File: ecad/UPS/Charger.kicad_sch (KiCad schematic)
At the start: 73 parts, among them J1 Barrel_Jack, J2 Conn_01x02_Socket, Q1 CSD18540Q5B, Q2 Q_PMOS_DGS, Q4 Q_PMOS_DGS, Q5 CSD18540Q5B, Q6 CSD18540Q5B, Q7 CSD18540Q5B, U1 BQ25730RSNR

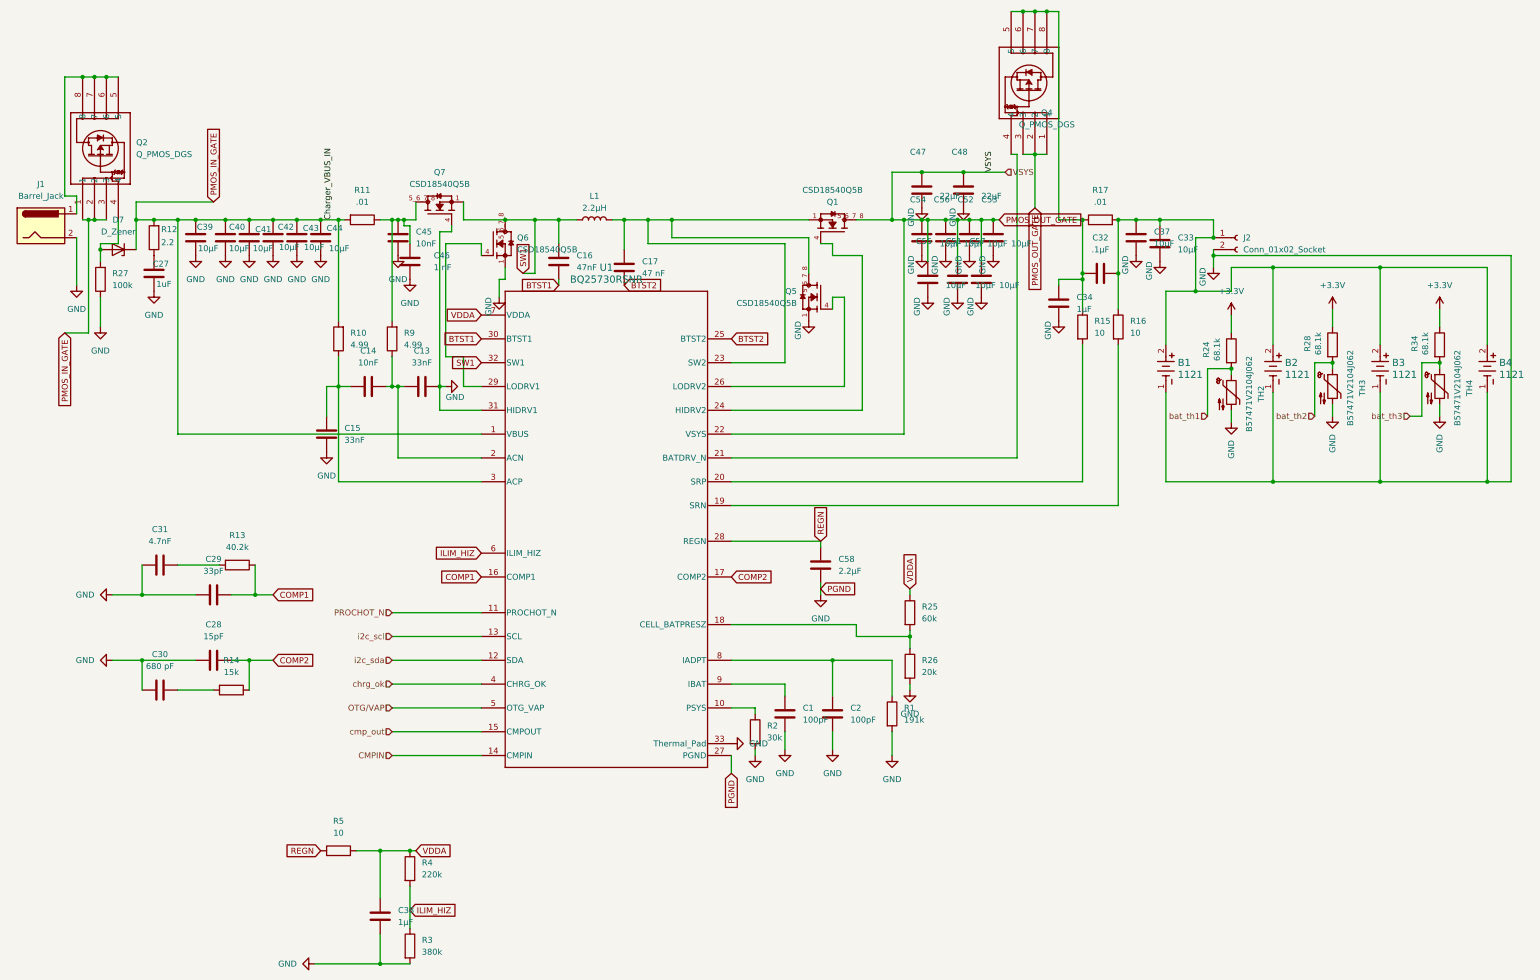
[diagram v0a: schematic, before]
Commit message: Did some routing, need to figure out how to route to BQ while appeasing DRC
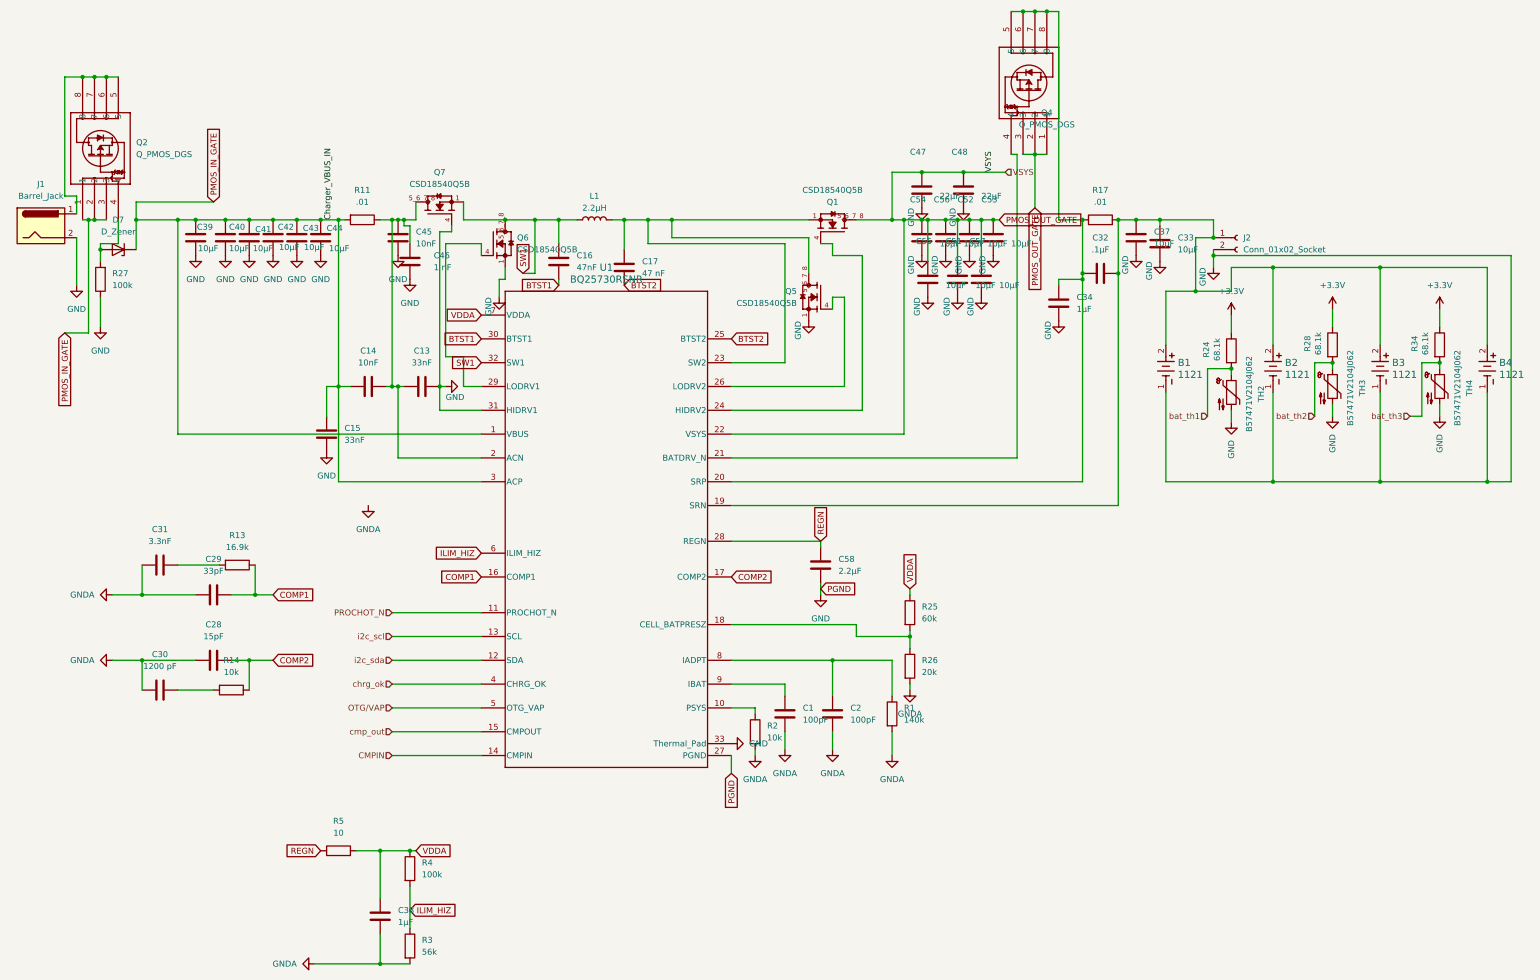
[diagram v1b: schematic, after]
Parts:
- removed C27: 1uF, Capacitor_SMD:C_0603_1608Metric, symbol Device:C
- removed R10, R9: 4.99, Resistor_SMD:R_0805_2012Metric, symbol Device:R
- removed R12: 2.2, Resistor_SMD:R_0805_2012Metric, symbol Device:R
- removed R15, R16: 10, Resistor_SMD:R_0805_2012Metric, symbol Device:R
- C30: value 680 pF -> 1200 pF
- C31: value 4.7nF -> 3.3nF
- Q4: footprint UPS:FDS6681Z_OSI-M -> UPS:FDS6681Z_OSI
- R1: value 191k -> 140k
- R13: value 40.2k -> 16.9k
- R14: value 15k -> 10k
- R2: value 30k -> 10k
- R3: value 380k -> 56k
- R4: value 220k -> 100k
- U1: footprint UPS:RSN0032B-IPC_A -> UPS:RSN0032B-IPC_C
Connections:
- net GND: no longer C1.2, C2.2, C28.1, C29.1, C30.1, C31.1, C38.2, R1.2, R2.2, R26.2, R3.2
- net PMOS_IN_GATE: now also C14.1, C15.2, U1.3 (ACP)
- net at B1.2, B2.2, B3.2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: now also U1.19 (SRN)
- net at C13.1, C14.2, U1.2 (ACN): now also C45.1, C46.1, Q7.5_6_7_8, R11.1
- net at C32.2, C34.1, Q4.5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: now also U1.20 (SRP)
- new net GNDA: C1.2, C2.2, C28.1, C29.1, C30.1, C31.1, C38.2, R1.2, R2.2, R26.2, R3.2

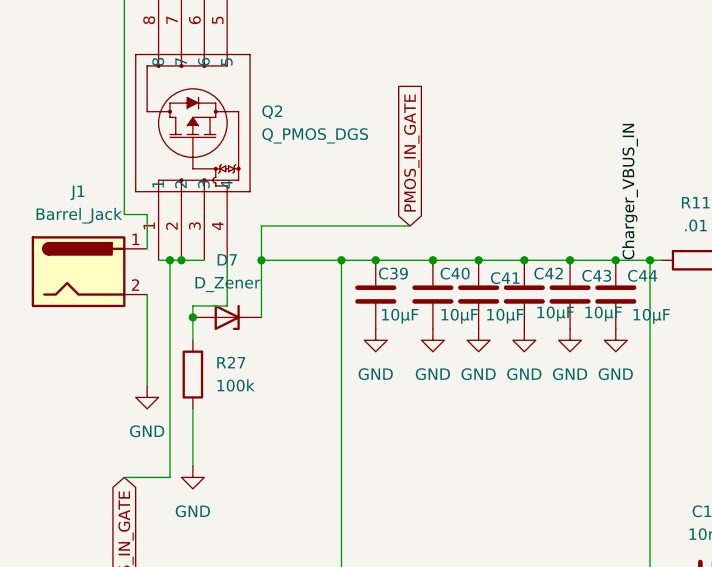
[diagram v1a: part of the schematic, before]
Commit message: Introduce fuses and a bit more routing
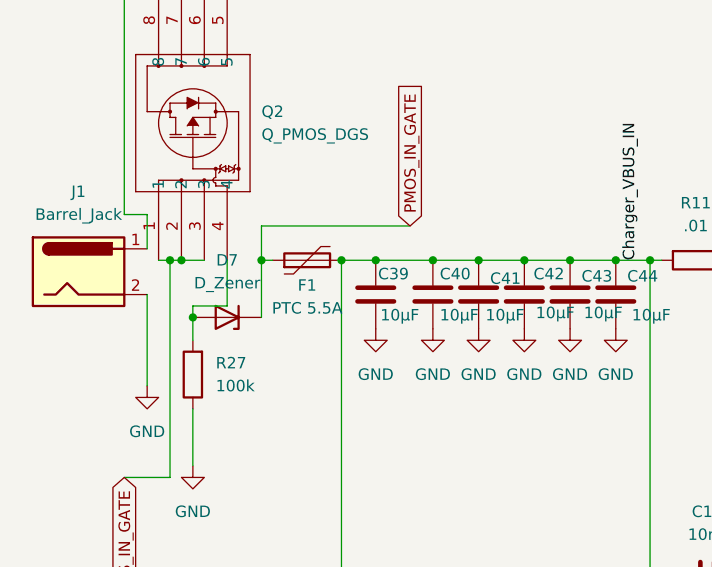
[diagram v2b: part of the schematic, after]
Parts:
- added F1: PTC 5.5A, Fuse:Fuse_1210_3225Metric_Pad1.42x2.65mm_HandSolder, symbol Device:Polyfuse
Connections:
- net PMOS_IN_GATE: now also F1.1; no longer C14.1, C15.2, C39.1, C40.1, C41.1, C42.1, C43.1, C44.1, R11.2, U1.1 (VBUS), U1.3 (ACP)
- new net Charger_VBUS_IN: C14.1, C15.2, C39.1, C40.1, C41.1, C42.1, C43.1, C44.1, F1.2, R11.2, U1.1 (VBUS), U1.3 (ACP)
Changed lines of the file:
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@@
 	)
 	(junction
+		(at 111.76 83.82)
+		(diameter 0)
+		(color 0 0 0 0)
+	)
+	(junction
 		(at 276.86 172.72)
 		(diameter 0)
@@
 	)
 	(junction
+		(at 120.65 83.82)
+		(diameter 0)
+		(color 0 0 0 0)
+	)
+	(junction
 		(at 303.53 69.85)
 		(diameter 0)
@@
 	)
 	(junction
-		(at 111.76 83.82)
-		(diameter 0)
-		(color 0 0 0 0)
-	)
-	(junction
 		(at 341.63 87.63)
 		(diameter 0)
@@
 	)
 	(junction
-		(at 120.65 83.82)
-		(diameter 0)
-		(color 0 0 0 0)
-	)
-	(junction
 		(at 377.19 93.98)
 		(diameter 0)
@@
 	(wire
 		(pts
-			(xy 111.76 83.82) (xy 120.65 83.82)
-		)
-		(stroke
-			(width 0)
-			(type default)
-		)
-	)
-	(wire
-		(pts
 			(xy 345.44 124.46) (xy 345.44 127)
 		)
@@
 	(wire
 		(pts
-			(xy 111.76 90.17) (xy 111.76 83.82)
-		)
-		(stroke
-			(width 0)
-			(type default)
-		)
-	)
-	(wire
-		(pts
 			(xy 177.8 88.9) (xy 185.42 88.9)
 		)
@@
 	(wire
 		(pts
+			(xy 111.76 83.82) (xy 113.03 83.82)
+		)
+		(stroke
+			(width 0)
+			(type default)
+		)
+	)
+	(wire
+		(pts
 			(xy 345.44 93.98) (xy 345.44 99.06)
 		)
@@
 	(wire
 		(pts
+			(xy 111.76 83.82) (xy 111.76 90.17)
+		)
+		(stroke
+			(width 0)
+			(type default)
+		)
+	)
+	(wire
+		(pts
 			(xy 167.64 119.38) (xy 168.91 119.38)
 		)
@@
 					(unit 1)
 				)
+			)
+		)
+	)
+	(symbol
+		(lib_id "Device:Polyfuse")
+		(at 116.84 83.82 90)
+		(unit 1)
+		(exclude_from_sim no)
+		(in_bom yes)
+		(on_board yes)
+		(dnp no)
+		(property "Reference" "F1"
+			(at 116.84 86.614 90)
+			(effects
+				(font
+					(size 1.27 1.27)
+				)
+			)
+		)
+		(property "Value" "PTC 5.5A"
+			(at 116.84 89.154 90)
+			(effects
+				(font
+					(size 1.27 1.27)
+				)
+			)
+		)
+		(property "Footprint" "Fuse:Fuse_1210_3225Metric_Pad1.42x2.65mm_HandSolder"
+			(at 121.92 82.55 0)
+			(effects
+				(font
+					(size 1.27 1.27)
+				)
+				(justify left)
+				(hide yes)
+			)
+		)
+		(property "Datasheet" "~"
+			(at 116.84 83.82 0)
+			(effects
+				(font
+					(size 1.27 1.27)
+				)
+				(hide yes)
+			)
+		)
+		(property "Description" "Resettable fuse, polymeric positive temperature coefficient"
+			(at 116.84 83.82 0)
+			(effects
+				(font
+					(size 1.27 1.27)
+				)
+				(hide yes)
+			)
+		)
+		(pin "1"
+		)
+		(pin "2"
+		)
+		(instances
+			(project ""
+				(path "/9d92b60a-4a6b-449c-b462-cab19e69d38c/58e8621a-e50a-4c31-8927-fd6b72ccb3ce"
+					(reference "F1")
+					(unit 1)
+				)

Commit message: More PCB Routing!!!!!
Most of the MCU is done
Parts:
- D7: value D_Zener -> 6V
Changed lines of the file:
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@@
 			)
 		)
-		(property "Value" "D_Zener"
+		(property "Value" "6V"
 			(at 107.95 86.36 0)
 			(effects

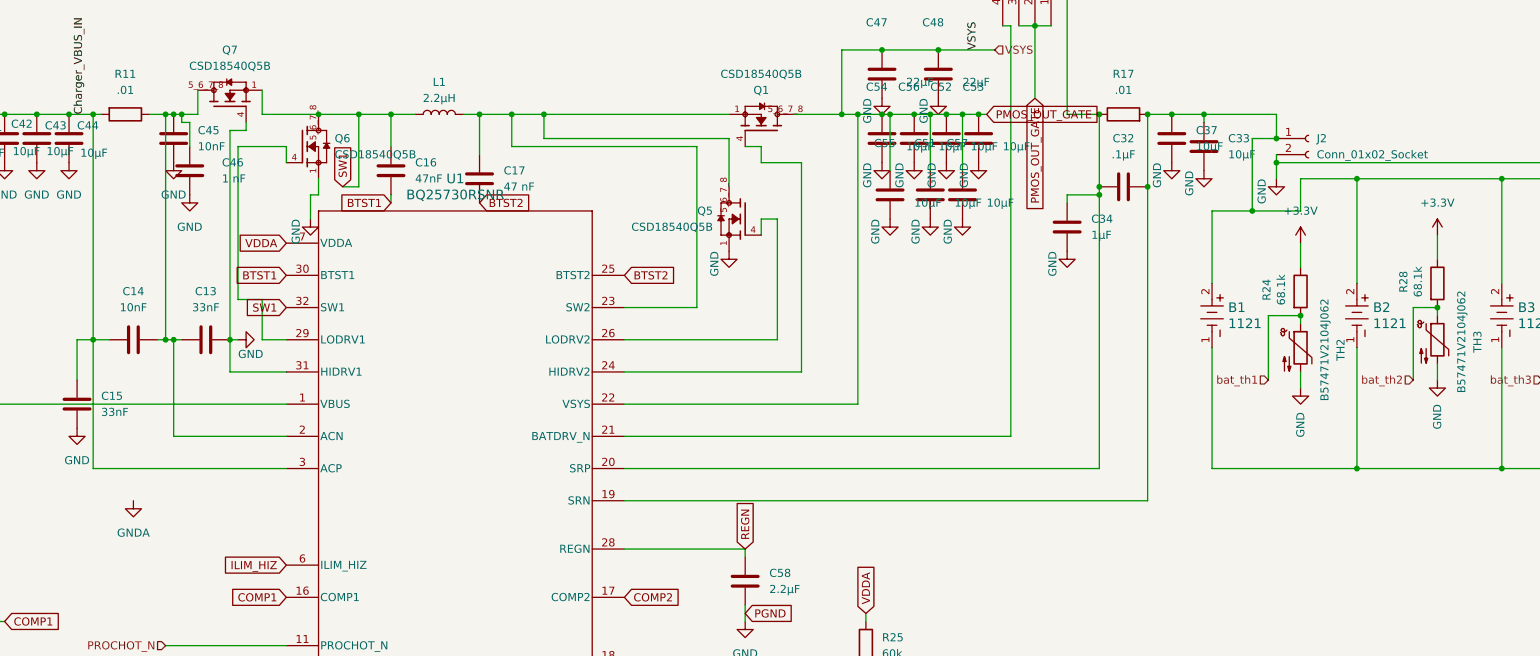
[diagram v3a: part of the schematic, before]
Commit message: VBATSENSE divider put in and some routing
Little more routing, complete by tonight
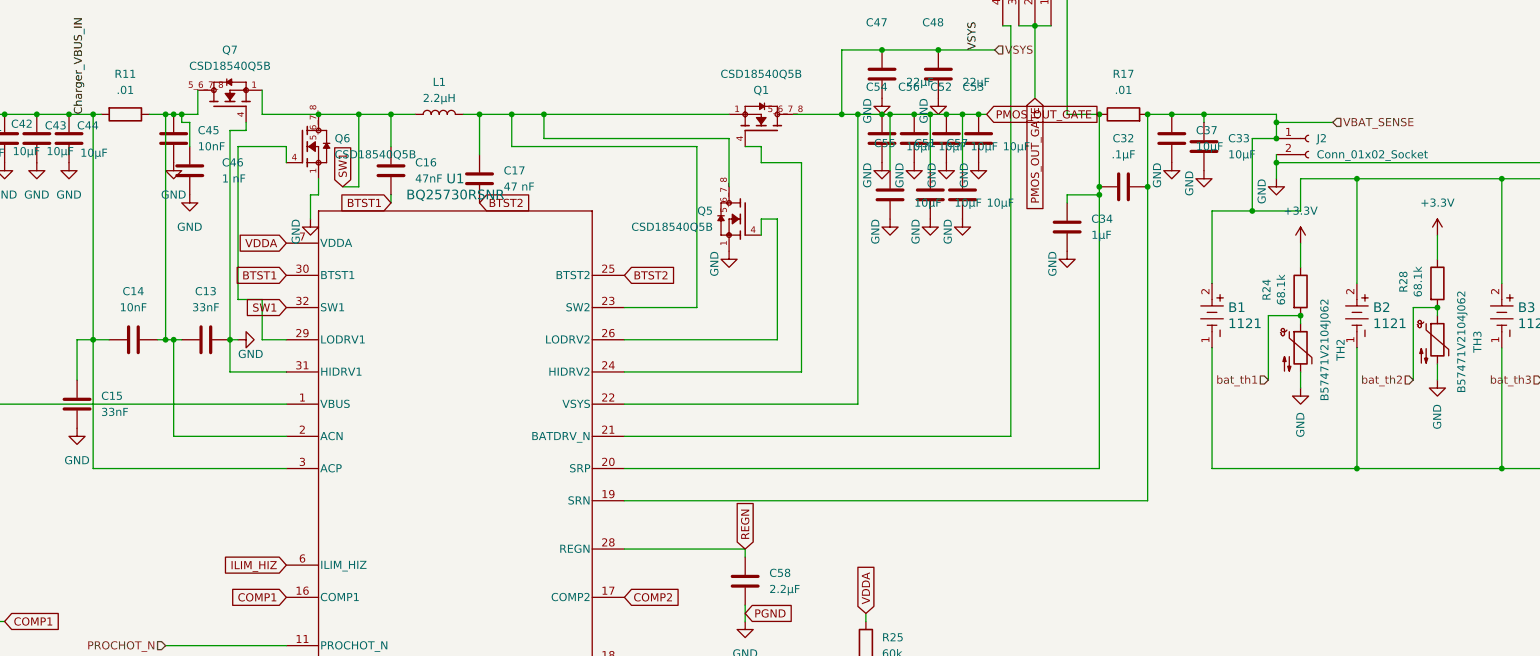
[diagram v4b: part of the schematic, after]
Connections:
- net VBAT_SENSE: now reaches B1.2, B2.2, B3.2, B4.2, C32.1, C33.1, C37.1, J2.1 (Pin_1), R17.2, U1.19 (SRN)
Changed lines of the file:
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@@
 	)
 	(junction
+		(at 341.63 85.09)
+		(diameter 0)
+		(color 0 0 0 0)
+	)
+	(junction
 		(at 113.03 177.8)
 		(diameter 0)
@@
 	(wire
 		(pts
+			(xy 341.63 85.09) (xy 341.63 83.82)
+		)
+		(stroke
+			(width 0)
+			(type default)
+		)
+	)
+	(wire
+		(pts
 			(xy 238.76 124.46) (xy 266.7 124.46)
 		)
@@
 	(wire
 		(pts
+			(xy 341.63 85.09) (xy 350.52 85.09)
+		)
+		(stroke
+			(width 0)
+			(type default)
+		)
+	)
+	(wire
+		(pts
 			(xy 166.37 193.04) (xy 185.42 193.04)
 		)
@@
 	(wire
 		(pts
-			(xy 341.63 87.63) (xy 341.63 83.82)
+			(xy 341.63 87.63) (xy 341.63 85.09)
 		)
 		(stroke
@@
 		)
 	)
+	(hierarchical_label "VBAT_SENSE"
+		(shape input)
+		(at 350.52 85.09 0)
+		(effects
+			(font
+				(size 1.27 1.27)
+			)
+			(justify left)
+		)
+	)
 	(symbol
 		(lib_id "UPS:1121")
@@
 					(unit 1)
 				)
-			)
-		)
-	)
-	(symbol
-		(lib_id "power:GNDA")
-		(at 161.29 144.78 0)
-		(unit 1)
-		(exclude_from_sim no)
-		(in_bom yes)
-		(on_board yes)
-		(dnp no)
-		(fields_autoplaced yes)
-		(property "Reference" "#PWR058"
-			(at 161.29 151.13 0)
-			(effects
-				(font
-					(size 1.27 1.27)
-				)
-				(hide yes)
-			)
-		)
-		(property "Value" "GNDA"
-			(at 161.29 149.86 0)
-			(effects
-				(font
-					(size 1.27 1.27)
-				)
-			)
-		)
-		(property "Footprint" ""
-			(at 161.29 144.78 0)
-			(effects
-				(font
-					(size 1.27 1.27)
-				)
-				(hide yes)
-			)
-		)
-		(property "Datasheet" ""
-			(at 161.29 144.78 0)
-			(effects
-				(font
-					(size 1.27 1.27)
-				)
-				(hide yes)
-			)
-		)
-		(property "Description" "Power symbol creates a global label with name \"GNDA\" , analog ground"
-			(at 161.29 144.78 0)
-			(effects
-				(font
-					(size 1.27 1.27)
-				)
-				(hide yes)
-			)
-		)
-		(pin "1"
-		)
-		(instances
-			(project "UPS"
-				(path "/9d92b60a-4a6b-449c-b462-cab19e69d38c/58e8621a-e50a-4c31-8927-fd6b72ccb3ce"
-					(reference "#PWR058")
-					(unit 1)
-				)
